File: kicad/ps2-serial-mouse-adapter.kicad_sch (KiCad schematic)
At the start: 8 parts, among them U1 Arduino_Nano, U2 MAX3232_HW027

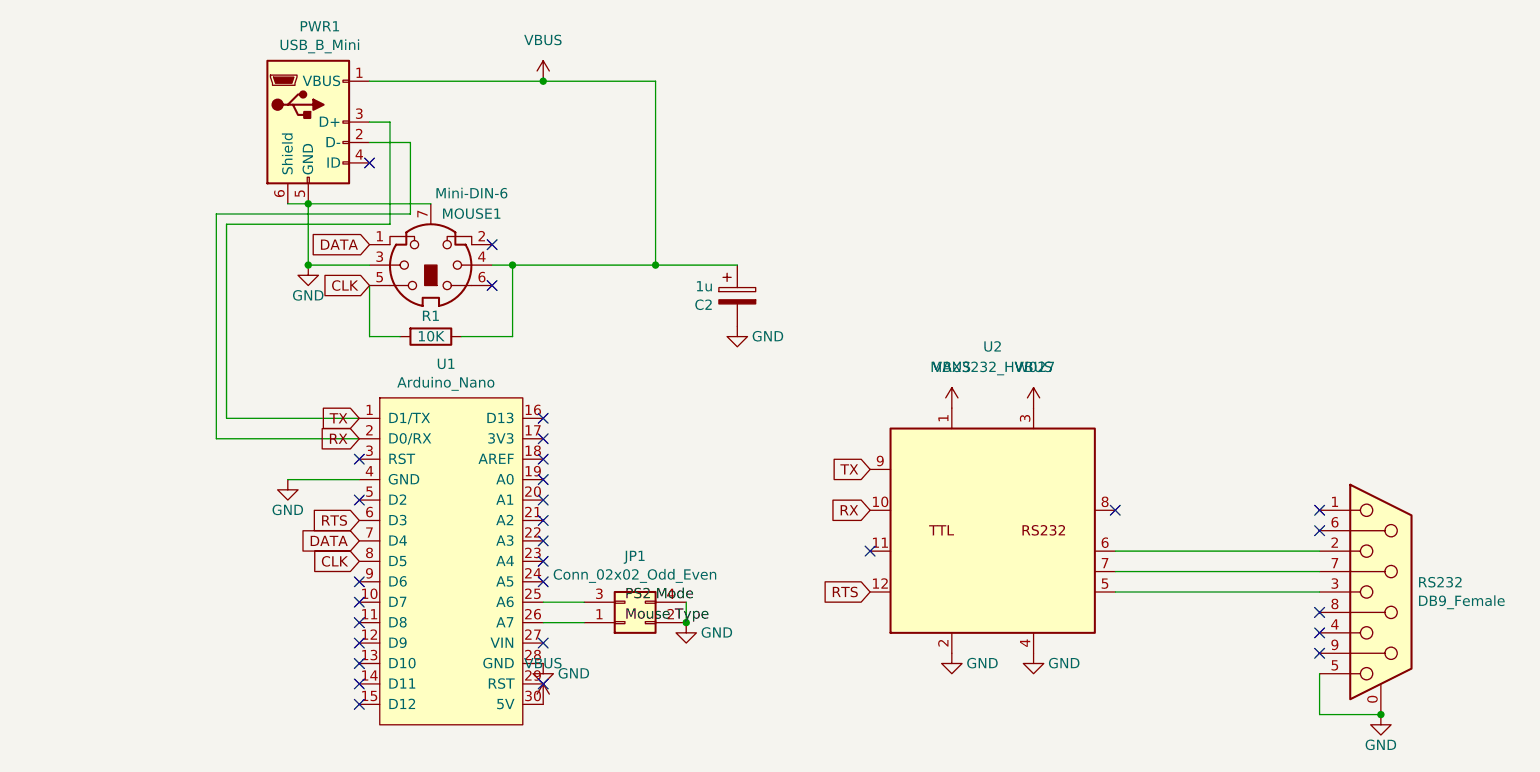
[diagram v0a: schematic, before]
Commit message: flip arduino and fix pinout. Change usb-mini plug to a pinheader row. Add pads for U2
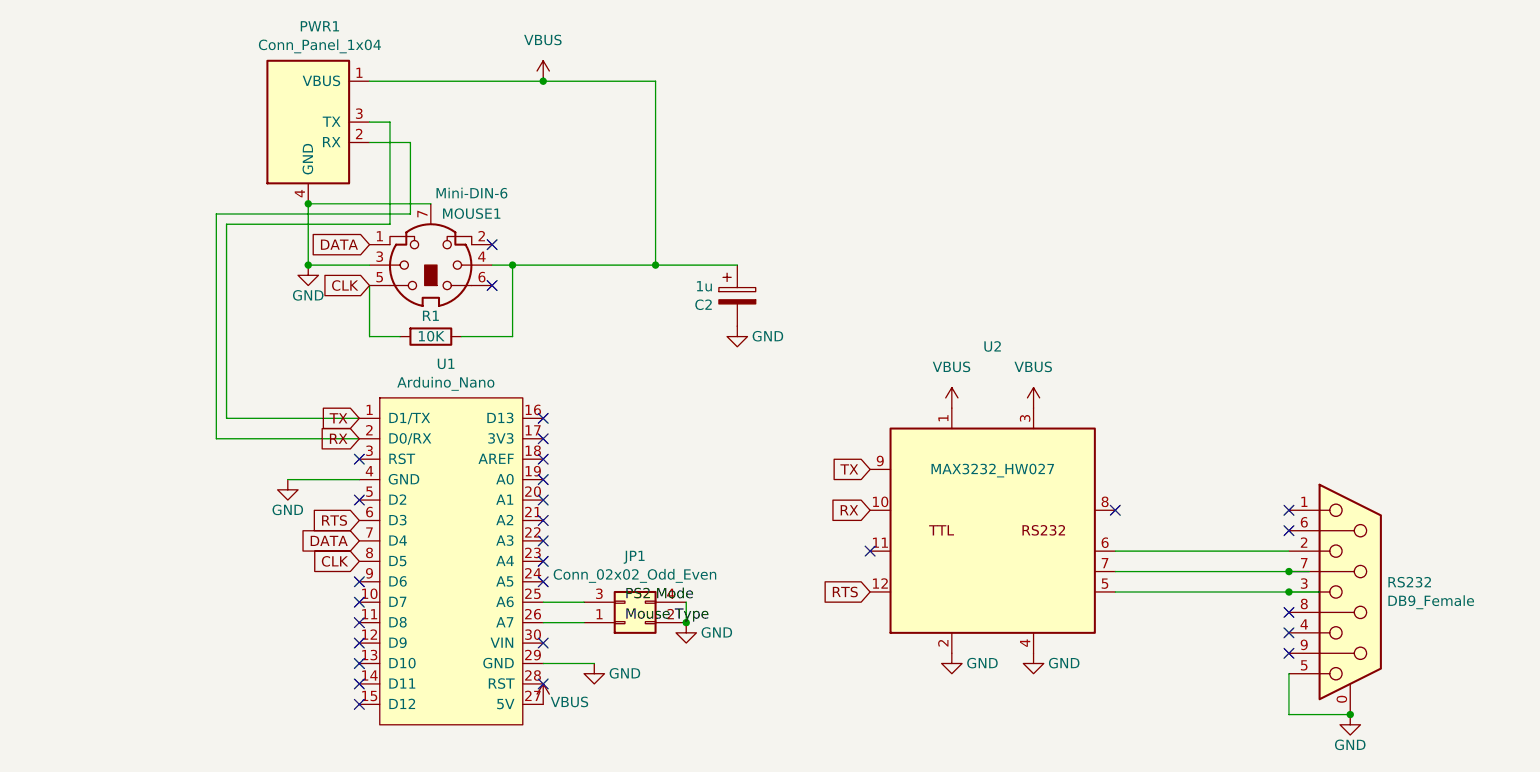
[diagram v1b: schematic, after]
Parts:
- PWR1: value USB_B_Mini -> Conn_Panel_1x04; footprint ps2-serial-mouse-adapter:USB_Mini-B-Jing_Extension_LSCS_C46398 -> Connector_PinHeader_2.54mm:PinHeader_1x04_P2.54mm_Vertical; symbol Connector:USB_B_Mini -> ps2-serial-mouse-adapter:Conn_Panel_1x04
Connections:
- net GND: now also PWR1.4 (GND), U1.29 (GND); no longer PWR1.5 (GND), PWR1.6 (Shield), U1.28 (GND)
- net VBUS: now also U1.27 (5V); no longer U1.30 (5V)
- no-connect marks 30 -> 29
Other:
- moved on the sheet: RS232
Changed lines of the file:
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@@
 	)
 	(junction
-		(at 208.28 116.84)
+		(at 204.47 116.84)
 		(diameter 0)
 		(color 0 0 0 0)
@@
 		(color 0 0 0 0)
 	)
+	(junction
+		(at 196.85 99.06)
+		(diameter 0)
+		(color 0 0 0 0)
+	)
+	(junction
+		(at 196.85 101.6)
+		(diameter 0)
+		(color 0 0 0 0)
+	)
 	(no_connect
 		(at 81.28 107.95)
@@
 	)
 	(no_connect
-		(at 200.66 93.98)
-	)
-	(no_connect
-		(at 200.66 91.44)
+		(at 196.85 93.98)
+	)
+	(no_connect
+		(at 196.85 91.44)
 	)
 	(no_connect
@@
 	)
 	(no_connect
-		(at 200.66 109.22)
+		(at 196.85 109.22)
 	)
 	(no_connect
@@
 	)
 	(no_connect
-		(at 200.66 104.14)
-	)
-	(no_connect
-		(at 200.66 106.68)
-	)
-	(no_connect
-		(at 82.55 48.26)
+		(at 196.85 104.14)
+	)
+	(no_connect
+		(at 196.85 106.68)
 	)
 	(wire
@@
 	(wire
 		(pts
-			(xy 72.39 53.34) (xy 74.93 53.34)
+			(xy 196.85 96.52) (xy 175.26 96.52)
+		)
+		(stroke
+			(width 0)
+			(type default)
+		)
+	)
+	(wire
+		(pts
+			(xy 196.85 101.6) (xy 175.26 101.6)
 		)
 		(stroke
@@
 	(wire
 		(pts
-			(xy 200.66 116.84) (xy 208.28 116.84)
+			(xy 196.85 99.06) (xy 175.26 99.06)
+		)
+		(stroke
+			(width 0)
+			(type default)
+		)
+	)
+	(wire
+		(pts
+			(xy 196.85 116.84) (xy 204.47 116.84)
 		)
 		(stroke
@@
 	(wire
 		(pts
-			(xy 200.66 111.76) (xy 200.66 116.84)
+			(xy 196.85 111.76) (xy 196.85 116.84)
 		)
 		(stroke
@@
 	(wire
 		(pts
-			(xy 175.26 96.52) (xy 200.66 96.52)
-		)
-		(stroke
-			(width 0)
-			(type default)
-		)
-	)
-	(wire
-		(pts
-			(xy 175.26 99.06) (xy 200.66 99.06)
-		)
-		(stroke
-			(width 0)
-			(type default)
-		)
-	)
-	(wire
-		(pts
-			(xy 175.26 101.6) (xy 200.66 101.6)
+			(xy 199.39 99.06) (xy 196.85 99.06)
+		)
+		(stroke
+			(width 0)
+			(type default)
+		)
+	)
+	(wire
+		(pts
+			(xy 200.66 101.6) (xy 196.85 101.6)
 		)
 		(stroke
@@
 		(pts
 			(xy 93.98 69.85) (xy 100.33 69.85)
+		)
+		(stroke
+			(width 0)
+			(type default)
+		)
+	)
+	(wire
+		(pts
+			(xy 110.49 110.49) (xy 104.14 110.49)
 		)
 		(stroke
@@
 	(symbol
 		(lib_id "power:GND")
-		(at 208.28 116.84 0)
+		(at 204.47 116.84 0)
 		(unit 1)
 		(body_style 1)
@@
 		(dnp no)
 		(property "Reference" "#PWR07"
-			(at 208.28 123.19 0)
+			(at 204.47 123.19 0)
 			(hide yes)
 			(show_name no)
@@
 		)
 		(property "Value" "GND"
-			(at 208.28 120.65 0)
+			(at 204.47 120.65 0)
 			(show_name no)
 			(do_not_autoplace no)
@@
 		)
 		(property "Footprint" ""
-			(at 208.28 116.84 0)
+			(at 204.47 116.84 0)
 			(hide yes)
 			(show_name no)
@@
 		)
 		(property "Datasheet" ""
-			(at 208.28 116.84 0)
+			(at 204.47 116.84 0)
 			(hide yes)
 			(show_name no)
@@
 		)
 		(property "Description" ""
-			(at 208.28 116.84 0)
+			(at 204.47 116.84 0)
 			(show_name no)
 			(do_not_autoplace no)
@@
 		)
 		(property "Value" "MAX3232_HW027"
-			(at 160.02 73.66 0)
+			(at 160.02 86.36 0)
 			(show_name no)
 			(do_not_autoplace no)
@@
 	(symbol
 		(lib_id "Connector:DB9_Female_MountingHoles")
-		(at 208.28 101.6 0)
+		(at 204.47 101.6 0)
 		(unit 1)
 		(body_style 1)
@@
 		(dnp no)
 		(property "Reference" "RS232"
-			(at 212.852 100.4316 0)
+			(at 209.042 100.4316 0)
 			(show_name no)
 			(do_not_autoplace no)
@@
 		)
 		(property "Value" "DB9_Female"
-			(at 212.852 102.743 0)
+			(at 209.042 102.743 0)
 			(show_name no)
 			(do_not_autoplace no)
@@
 		)
 		(property "Footprint" "Connector_Dsub:DSUB-9_Female_Horizontal_P2.77x2.84mm_EdgePinOffset7.70mm_Housed_MountingHolesOffset9.12mm"
-			(at 208.28 101.6 0)
+			(at 204.47 101.6 0)
 			(hide yes)
 			(show_name no)
@@
 		)
 		(property "Datasheet" "~"
-			(at 208.28 101.6 0)
+			(at 204.47 101.6 0)
 			(hide yes)
 			(show_name no)
@@
 		)
 		(property "Description" ""
-			(at 208.28 101.6 0)
+			(at 204.47 101.6 0)
 			(show_name no)
 			(do_not_autoplace no)
@@
 	)
 	(symbol
-		(lib_id "Connector:USB_B_Mini")
+		(lib_id "ps2-serial-mouse-adapter:Conn_Panel_1x04")
 		(at 74.93 43.18 0)
 		(unit 1)
@@
 			)
 		)
-		(property "Value" "USB_B_Mini"
+		(property "Value" "Conn_Panel_1x04"
 			(at 76.3778 33.6296 0)
 			(show_name no)
@@
 			)
 		)
-		(property "Footprint" "ps2-serial-mouse-adapter:USB_Mini-B-Jing_Extension_LSCS_C46398"
+		(property "Footprint" "Connector_PinHeader_2.54mm:PinHeader_1x04_P2.54mm_Vertical"
 			(at 78.74 44.45 0)
 			(hide yes)
@@
 		)
 		(pin "4"
-		)
-		(pin "5"
-		)
-		(pin "6"
 		)
 		(instances
@@
 	(symbol
 		(lib_id "power:GND")
-		(at 104.14 110.49 0)
+		(at 110.49 110.49 0)
 		(unit 1)
 		(body_style 1)
@@
 		(dnp no)
 		(property "Reference" "#PWR10"
-			(at 104.14 116.84 0)
+			(at 110.49 116.84 0)
 			(hide yes)
 			(show_name no)
@@
 		)
 		(property "Value" "GND"
-			(at 107.95 111.76 0)
+			(at 114.3 111.76 0)
 			(show_name no)
 			(do_not_autoplace no)
@@
 		)
 		(property "Footprint" ""
-			(at 104.14 110.49 0)
+			(at 110.49 110.49 0)
 			(hide yes)
 			(show_name no)
@@
 		)
 		(property "Datasheet" ""
-			(at 104.14 110.49 0)
+			(at 110.49 110.49 0)
 			(hide yes)
 			(show_name no)
@@
 		)
 		(property "Description" ""
-			(at 104.14 110.49 0)
+			(at 110.49 110.49 0)
 			(show_name no)
 			(do_not_autoplace no)
@@
 		(in_pos_files yes)
 		(dnp no)
-		(fields_autoplaced yes)
 		(property "Reference" "#PWR05"
 			(at 104.14 119.38 0)
@@
 		)
 		(property "Value" "VBUS"
-			(at 104.14 110.49 0)
-			(show_name no)
-			(do_not_autoplace no)
+			(at 107.442 115.316 0)
+			(show_name no)
+			(do_not_autoplace no)

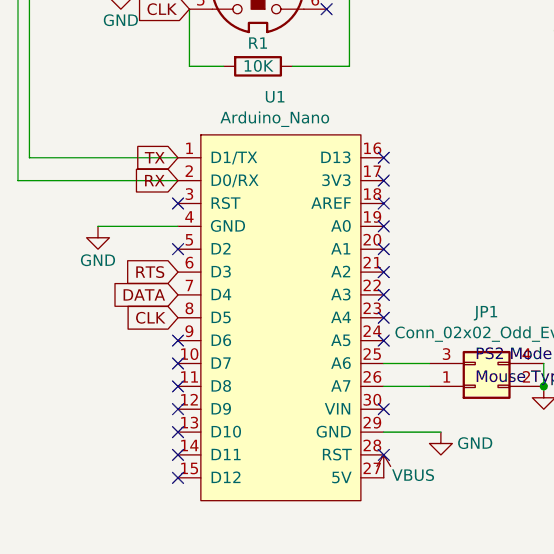
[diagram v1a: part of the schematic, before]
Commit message: Fix positioning of no_connect and global_label in PS2 Serial Mouse Adapter schematic
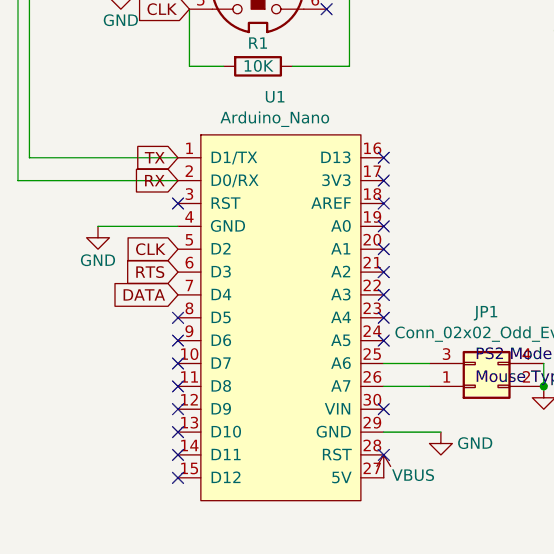
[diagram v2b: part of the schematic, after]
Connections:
- net CLK: now also U1.5 (D2); no longer U1.8 (D5)
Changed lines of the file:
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@@
 	)
 	(no_connect
-		(at 81.28 90.17)
+		(at 81.28 97.79)
 	)
 	(no_connect
@@
 	(global_label "CLK"
 		(shape input)
-		(at 81.28 97.79 180)
+		(at 81.28 90.17 180)
 		(fields_autoplaced yes)
 		(effects

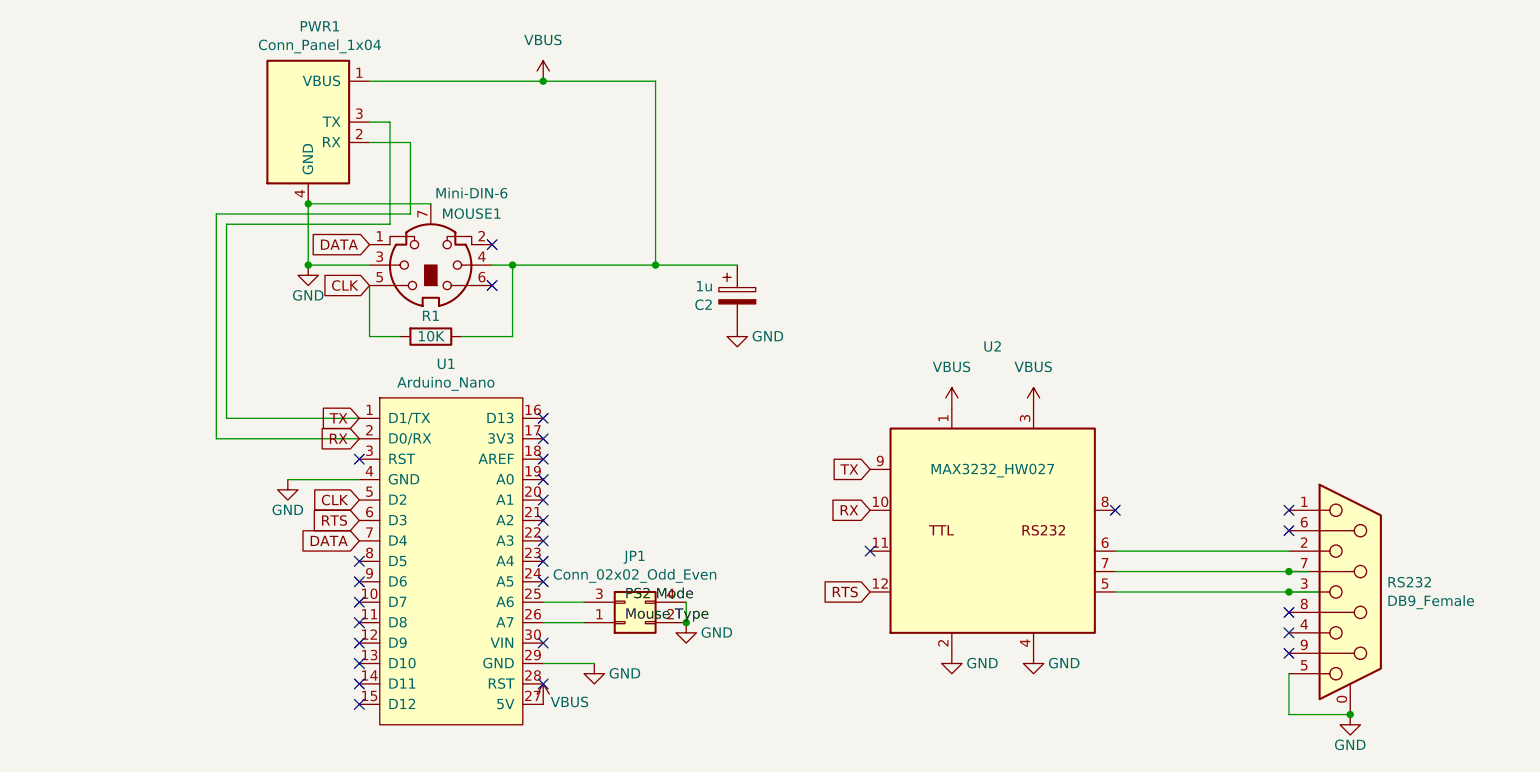
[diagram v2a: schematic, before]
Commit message: Refactor code structure for improved readability and maintainability. Removed unused Rx from design, unused for this purpose. Added activity LEDs for pre and post MAX232 on TX. Aditional bipolar filter cap on Vcc and pull up resistor on Data line. Added debug mode  jumper.
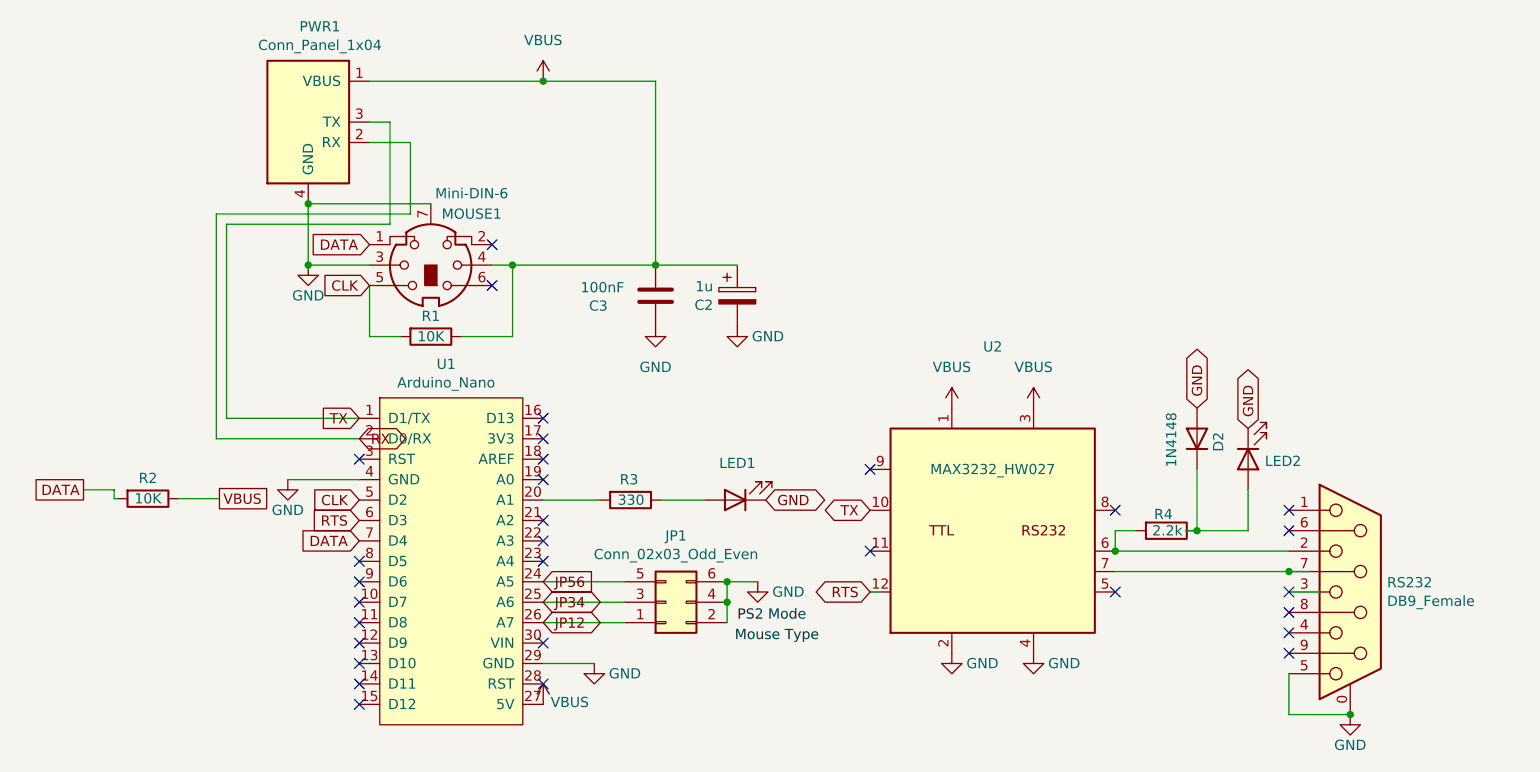
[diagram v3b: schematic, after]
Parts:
- added C3: 100nF, Capacitor_THT:C_Disc_D3.0mm_W1.6mm_P2.50mm, symbol Device:C
- added D2: 1N4148, Diode_THT:D_DO-35_SOD27_P7.62mm_Horizontal, symbol Device:D
- added LED1, LED2: LED, LED_THT:LED_D3.0mm, symbol Device:LED
- added R2: 10K, Resistor_THT:R_Axial_DIN0207_L6.3mm_D2.5mm_P7.62mm_Horizontal, symbol Device:R
- added R3: 330, Resistor_THT:R_Axial_DIN0207_L6.3mm_D2.5mm_P7.62mm_Horizontal, symbol Device:R
- added R4: 2.2k, Resistor_THT:R_Axial_DIN0207_L6.3mm_D2.5mm_P7.62mm_Horizontal, symbol Device:R
- JP1: value Conn_02x02_Odd_Even -> Conn_02x03_Odd_Even; symbol Connector_Generic:Conn_02x02_Odd_Even -> Connector_Generic:Conn_02x03_Odd_Even
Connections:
- net DATA: now also R2.2
- net GND: now also JP1.6 (Pin_6), C3.2, D2.2 (A), LED1.1 (K), LED2.1 (K)
- net RX: no longer U2.10 (TTL_RXD1)
- net TX: now also U2.10 (TTL_RXD1); no longer U2.9 (TTL_TXD1)
- net VBUS: now also C3.1, R2.1
- net at U1.20 (A1): now also R3.2
- net JP56: now reaches U1.24 (A5)
- net JP56: now also JP1.5 (Pin_5)
- net JP34: now reaches JP1.3 (Pin_3), U1.25 (A6)
- net JP12: now reaches JP1.1 (Pin_1), U1.26 (A7)
- net at U2.5 (RS232_RXD1): no longer RS232.3
- net at RS232.2, U2.6 (RS232_TXD1): now also R4.2
- new net: D2.1 (K), LED2.2 (A), R4.1
- new net: LED1.2 (A), R3.1
- no-connect marks 29 -> 30
